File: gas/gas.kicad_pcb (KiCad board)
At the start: 2 copper layers, 105.4 x 95.2 mm, 23 parts, among them J1 Conn_01x38_Male, J2 Screw_Terminal_01x09, J3 Screw_Terminal_01x09, K1 G5LE-1-E, K2 G5LE-1-E, K3 G5LE-1-E, K4 G5LE-1-E, K5 G5LE-1-E, K6 G5LE-1-E, U1 ESP32-DevKitC, U2 ULN2003A

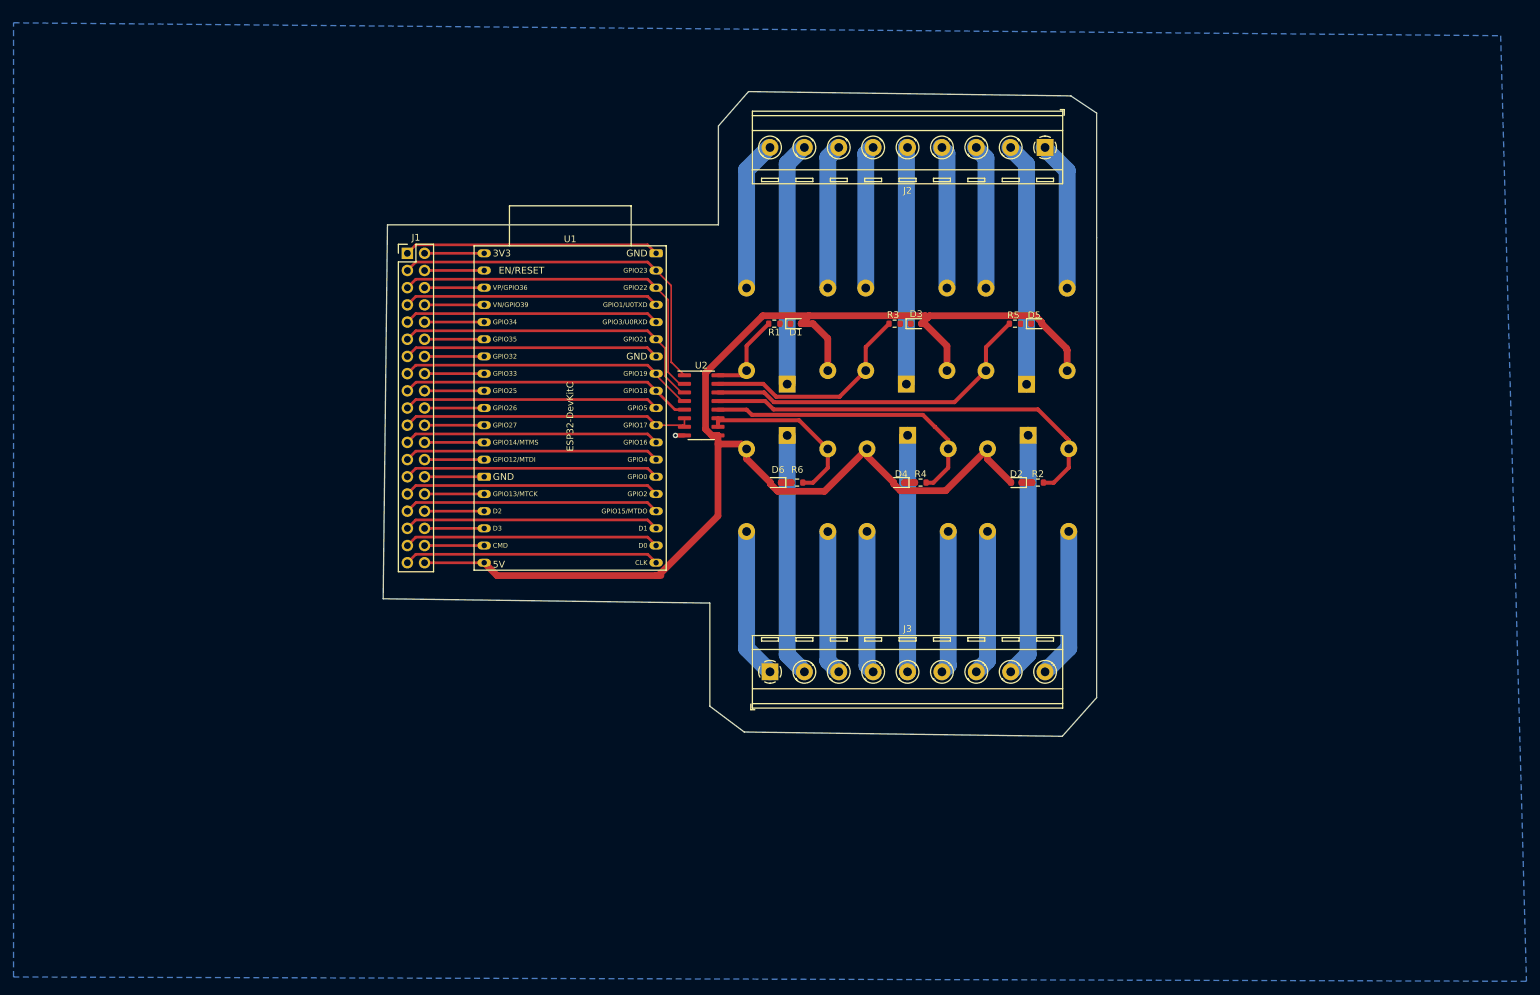
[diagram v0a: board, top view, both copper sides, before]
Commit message: feat: pcb update, box init
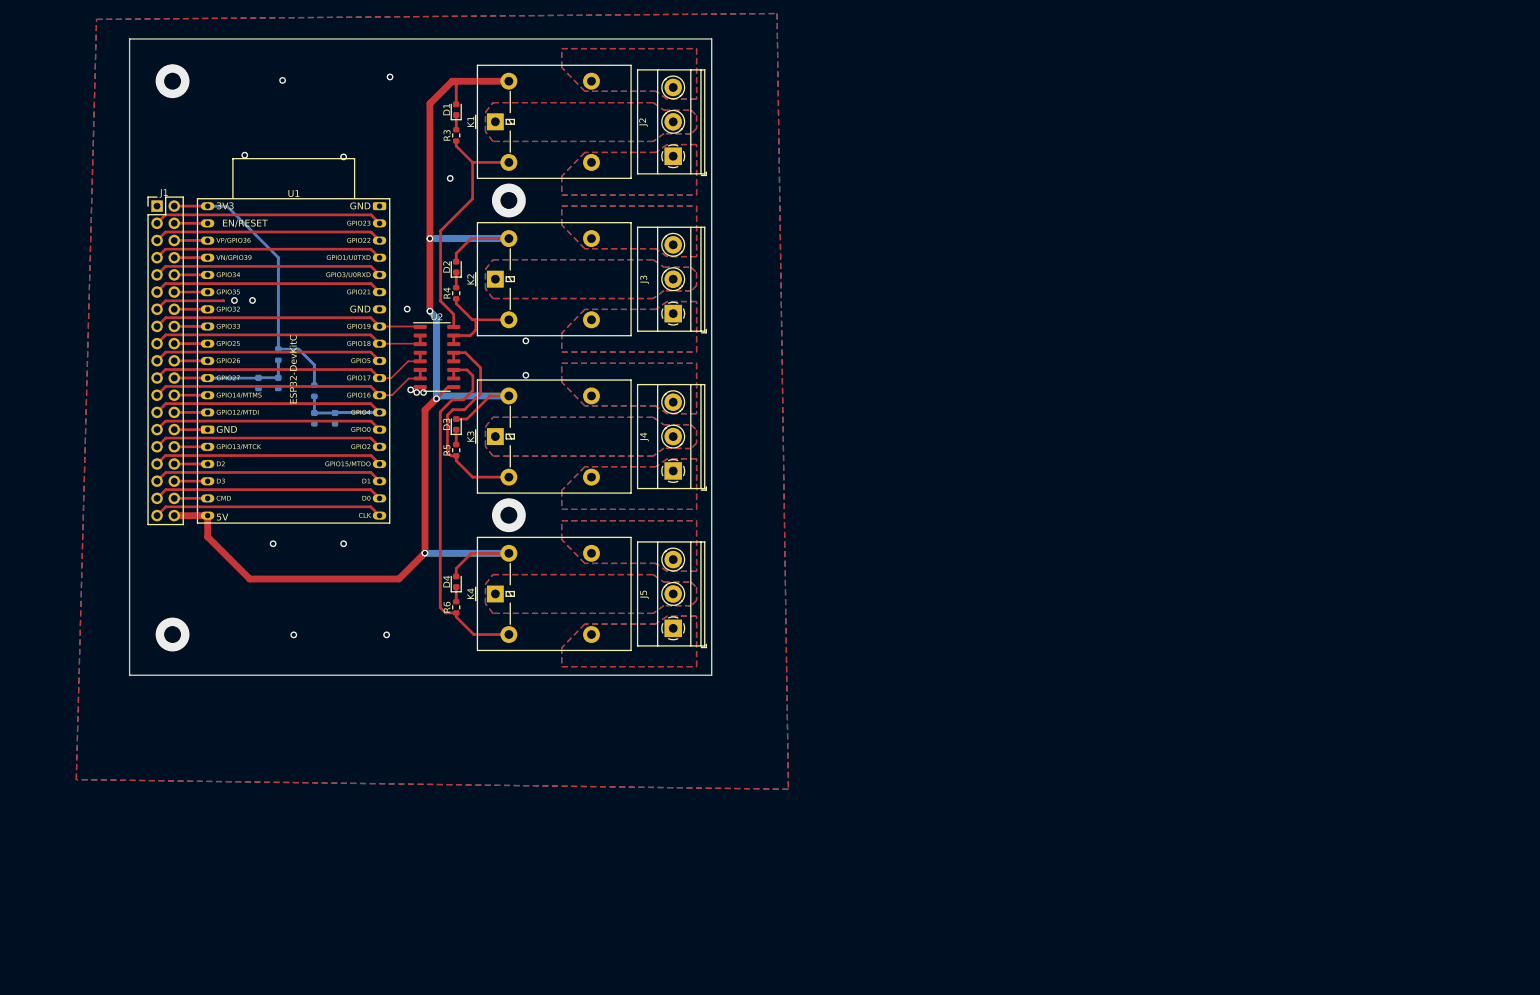
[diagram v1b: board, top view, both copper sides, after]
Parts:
- removed D5, D6: LED, LED_SMD:LED_0603_1608Metric
- removed K5, K6: G5LE-1-E, Relay_THT:Relay_SPDT_Omron-G5LE-1
- added C1: C, Capacitor_SMD:C_0603_1608Metric, B.Cu at (74.8, 76.2)
- added C2: C, Capacitor_SMD:C_0603_1608Metric, B.Cu at (63.5, 71.0)
- added J4: Screw_Terminal_01x03, TerminalBlock_Phoenix:TerminalBlock_Phoenix_MKDS-1,5-3-5.08_1x03_P5.08mm_Horizontal, F.Cu at (124.8, 84.0)
- added J5: Screw_Terminal_01x03, TerminalBlock_Phoenix:TerminalBlock_Phoenix_MKDS-1,5-3-5.08_1x03_P5.08mm_Horizontal, F.Cu at (124.8, 107.2)
- added TH1: Thermistor_NTC, Resistor_SMD:R_0603_1608Metric, B.Cu at (66.4, 66.8)
- added TH2: Thermistor_NTC, Resistor_SMD:R_0603_1608Metric, B.Cu at (71.8, 72.1)
- J2, J3: value Screw_Terminal_01x09 -> Screw_Terminal_01x03; footprint TerminalBlock_RND:TerminalBlock_RND_205-00294_1x09_P5.08mm_Horizontal -> TerminalBlock_Phoenix:TerminalBlock_Phoenix_MKDS-1,5-3-5.08_1x03_P5.08mm_Horizontal
- K1, K2, K3, K4: moved to F.Cu
- R1, R2: value 120R -> R; footprint Resistor_SMD:R_0603_1608Metric -> Capacitor_SMD:C_0603_1608Metric; moved to B.Cu
- moved R2 107.3 mm to (71.8, 76.2), turned to -90 degrees
- moved D2 88.7 mm to (92.7, 53.9), turned to 90 degrees
- moved R5 84.6 mm to (92.7, 80.9), turned to -90 degrees
- moved K2 82.0 mm to (98.5, 55.7), turned to 90 degrees
- moved R4 74.1 mm to (92.7, 57.7), turned to -90 degrees
- moved R1 73.8 mm to (66.4, 71.0), turned to -90 degrees
- moved R3 70.5 mm to (92.7, 34.4), turned to -90 degrees
- moved D3 69.6 mm to (92.7, 77.1), turned to 90 degrees
- moved D4 67.0 mm to (92.7, 100.4), turned to 90 degrees
- moved K4 65.3 mm to (98.5, 102.2), turned to 90 degrees
- moved K3 61.2 mm to (98.5, 78.9), turned to 90 degrees
- moved D1 59.3 mm to (92.7, 30.6), turned to 90 degrees
- moved K1 58.0 mm to (98.5, 32.4), turned to 90 degrees
- moved J2 55.0 mm to (124.8, 37.5), turned to 90 degrees
- moved J3 54.8 mm to (124.8, 60.7), turned to 90 degrees
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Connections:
- J3 pad 1: O10 -> O4
- J3 pad 2: O11 -> O5
- J3 pad 3: O12 -> O6
- K1 pad 1: O8 -> O2
- K1 pad 3: O9 -> O1
- K1 pad 4: O7 -> O3
- K2 pad 1: O17 -> O5
- K2 pad 3: O18 -> O4
- K2 pad 4: O16 -> O6
- K3 pad 1: O5 -> O8
- K3 pad 3: O6 -> O7
- K3 pad 4: O4 -> O9
- K4 pad 1: O14 -> O11
- K4 pad 3: O15 -> O10
- K4 pad 4: O13 -> O12
- R1 pad 1: Net-(D1-Pad1) -> /U11
- R1 pad 2: Net-(K1-Pad2) -> GND
- R2 pad 1: Net-(D2-Pad1) -> /U26
- R2 pad 2: Net-(K2-Pad2) -> GND
- R3 pad 1: Net-(D3-Pad1) -> Net-(D1-Pad1)
- R3 pad 2: Net-(K3-Pad2) -> Net-(K1-Pad2)
- R4 pad 1: Net-(D4-Pad1) -> Net-(D2-Pad1)
- R4 pad 2: Net-(K4-Pad2) -> Net-(K2-Pad2)
- R5 pad 1: Net-(D5-Pad1) -> Net-(D3-Pad1)
- R5 pad 2: Net-(K5-Pad2) -> Net-(K3-Pad2)
- R6 pad 1: Net-(D6-Pad1) -> Net-(D4-Pad1)
- R6 pad 2: Net-(K6-Pad2) -> Net-(K4-Pad2)
- U2 pad 1: /U37 -> /U31
- U2 pad 10: Net-(K6-Pad2) -> Net-(K4-Pad2)
- U2 pad 11: Net-(K6-Pad2) -> Net-(K4-Pad2)
- U2 pad 12: Net-(K4-Pad2) -> Net-(K3-Pad2)
- U2 pad 13: Net-(K2-Pad2) -> Net-(K3-Pad2)
- U2 pad 14: Net-(K5-Pad2) -> Net-(K2-Pad2)
- U2 pad 15: Net-(K3-Pad2) -> Net-(K2-Pad2)
- U2 pad 2: /U36 -> /U30
- U2 pad 3: /U33 -> /U30
- U2 pad 4: /U31 -> /U28
- U2 pad 5: /U30 -> /U28
- U2 pad 6: /U28 -> /U27
- U2 pad 7: /U28 -> /U27
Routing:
- net GND: track 85.7 -> 15.3 mm, vias 1 -> 21
- net Net-(K5-Pad2): track 50.5 -> 0.00 mm
- net Net-(K2-Pad2): track 62.9 -> 15.9 mm
- net O2: track 36.0 -> 0.00 mm
- net O17: track 36.0 -> 0.00 mm
- net O11: track 36.0 -> 0.00 mm
- net O8: track 36.0 -> 0.00 mm
- net O5: track 35.0 -> 0.00 mm
- net O14: track 35.0 -> 0.00 mm
- net +3V3: track 8.81 -> 41.3 mm
- net Net-(K6-Pad2): track 26.8 -> 0.00 mm
- net Net-(K1-Pad2): track 12.8 -> 36.6 mm
- net O1: track 22.2 -> 0.00 mm
- net O18: track 22.2 -> 0.00 mm
- net O10: track 22.2 -> 0.00 mm
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- added copper zone on F.Cu, net GND
- added copper zone on B.Cu, net O1
- added copper zone on F.Cu, net O1
- added copper zone on B.Cu, net O10
- added copper zone on F.Cu, net O10
- added copper zone on B.Cu, net O11
- added copper zone on F.Cu, net O11
- added copper zone on B.Cu, net O12
- added copper zone on F.Cu, net O12
- added copper zone on B.Cu, net O2
- added copper zone on F.Cu, net O2
- added copper zone on B.Cu, net O3
- added copper zone on F.Cu, net O3
- added copper zone on B.Cu, net O4
- added copper zone on F.Cu, net O4
- added copper zone on B.Cu, net O5
- added copper zone on F.Cu, net O5
- added copper zone on B.Cu, net O6
- added copper zone on F.Cu, net O6
- added copper zone on B.Cu, net O7
- added copper zone on F.Cu, net O7
- added copper zone on B.Cu, net O8
- added copper zone on F.Cu, net O8
- added copper zone on B.Cu, net O9
- added copper zone on F.Cu, net O9
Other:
- board size 105.4 x 95.2 mm -> 86 x 94 mm
